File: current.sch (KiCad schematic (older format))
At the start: 35 parts

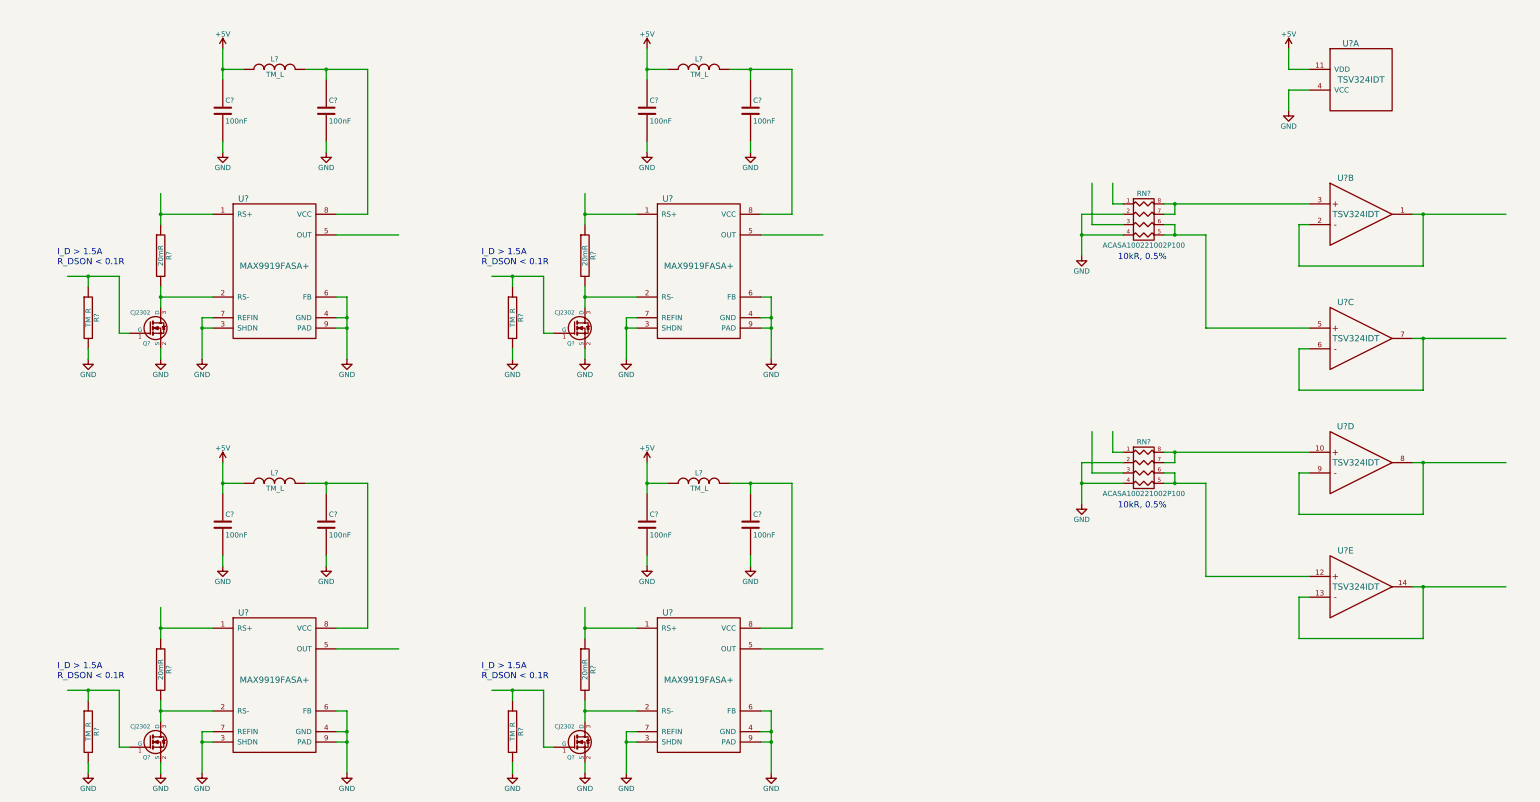
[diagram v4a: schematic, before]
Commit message: connected analog things, lots of testpoints
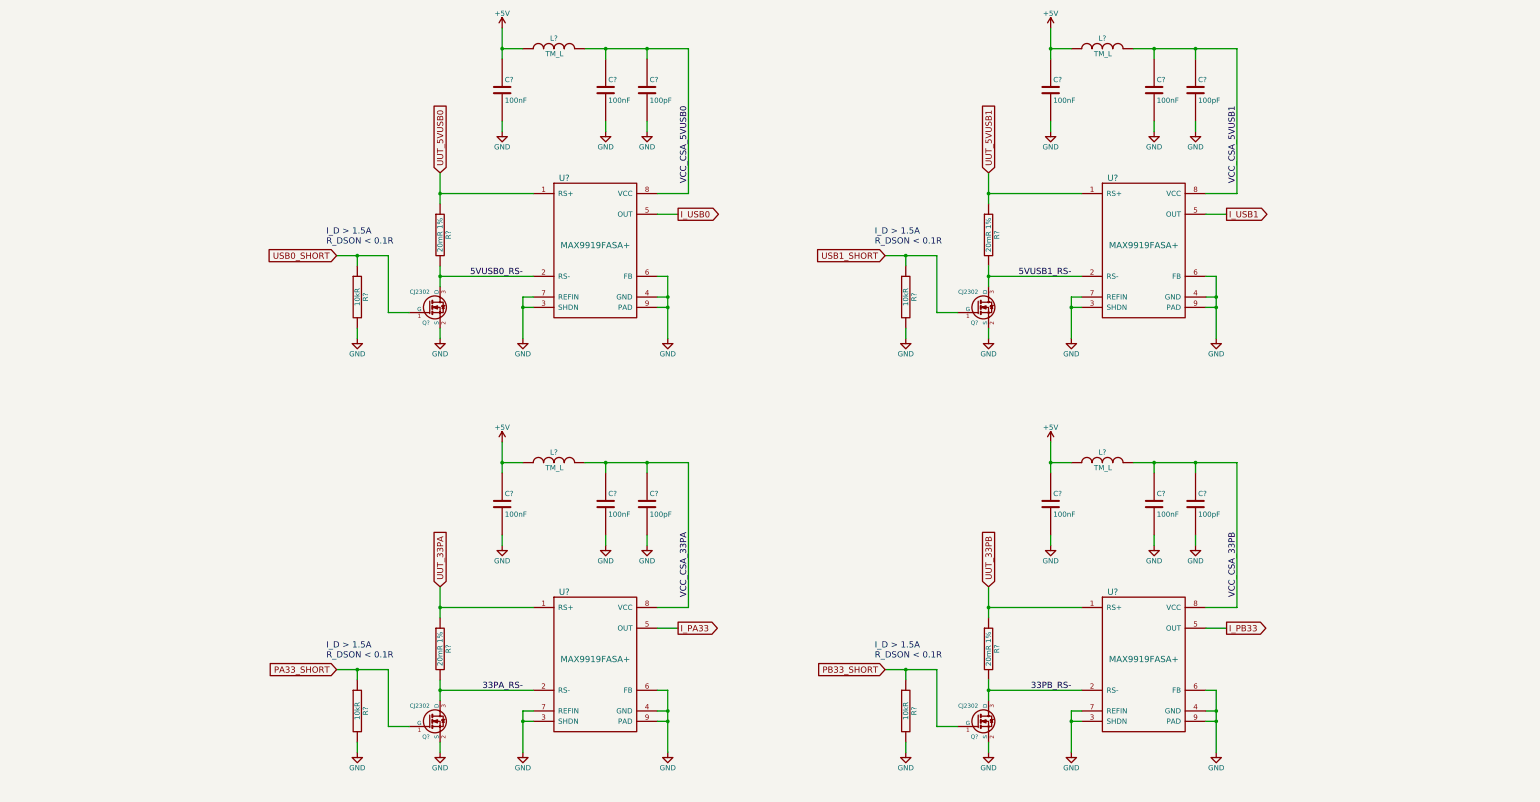
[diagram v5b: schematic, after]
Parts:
- removed C? (x6): 100nF, symbol TM_C
- removed L? (x3): TM_L, symbol TM_L
- removed RN? (x2): ACASA100221002P100, symbol R_PACK4
- removed U? (x5): TSV324IDT, symbol TSV324IDT
- added C? (x4): 100pF, symbol TM_C
- added C? (x6): 100nF, symbol TM_C
- added L? (x3): TM_L, symbol TM_L
- R? (x4): value 20mR -> 20mR 1%
- R? (x4): value TM_R -> 10kR
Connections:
- net labels added: 33PA_RS-, 33PB_RS-, 5VUSB0_RS-, 5VUSB1_RS-, I_PA33, I_PB33, I_USB0, I_USB1, PA33_SHORT, PB33_SHORT, USB0_SHORT, USB1_SHORT, UUT_33PA, UUT_33PB, UUT_5VUSB0, UUT_5VUSB1, VCC_CSA_33PA, VCC_CSA_33PB, VCC_CSA_5VUSB0, VCC_CSA_5VUSB1
- wire segments 158 -> 144
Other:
- note removed: "10kR, 0.5%"
- moved on the sheet: C?, L?, Q?, R?, U?

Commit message: schematic check with kevin. misc fixes, mostly on usb
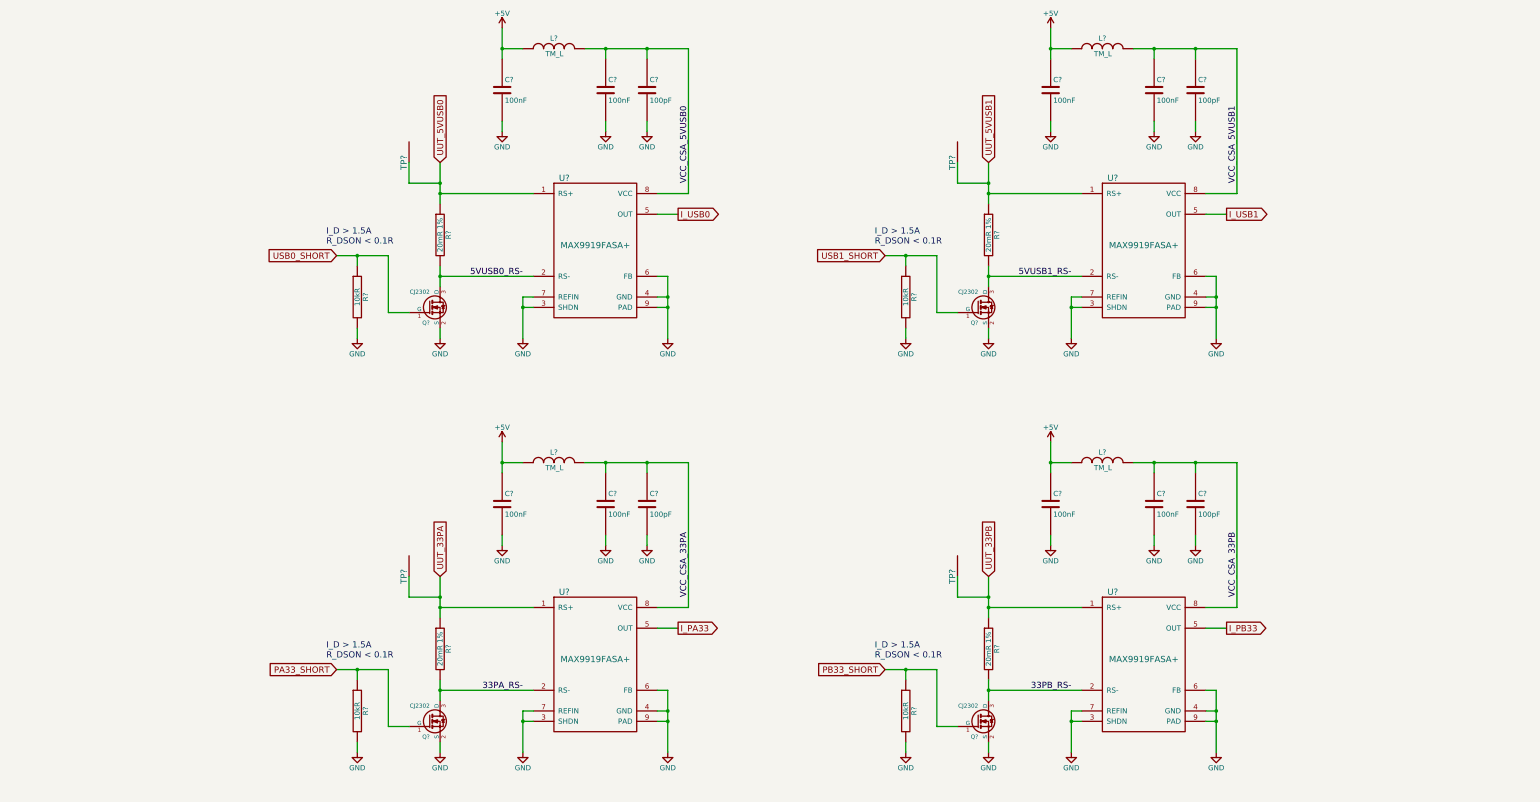
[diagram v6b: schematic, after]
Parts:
- added TP? (x4): TP, symbol TP
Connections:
- net UUT_33PA: now also TP?.~
- net UUT_33PB: now also TP?.~
- net UUT_5VUSB0: now also TP?.~
- net UUT_5VUSB1: now also TP?.~
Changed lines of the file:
@@
 	10600 3000 11500 3000
 Wire Wire Line
-	10600 2800 10600 3000
+	10600 2700 10600 2900
+Wire Wire Line
+	10600 2900 10600 3000
 Wire Wire Line
 	10600 3000 10600 3100
@@
 	5300 3000 6200 3000
 Wire Wire Line
-	5300 2800 5300 3000
+	5300 2700 5300 2900
+Wire Wire Line
+	5300 2900 5300 3000
 Wire Wire Line
 	5300 3000 5300 3100
@@
 	6700 1600 6900 1600
 Wire Wire Line
-	6900 1600 7700 1600
+	6900 1600 7300 1600
+Wire Wire Line
+	7300 1600 7700 1600
 Connection ~ 6900 1600
 Connection ~ 5300 3800
@@
 	5300 7000 6200 7000
 Wire Wire Line
-	5300 6800 5300 7000
+	5300 6700 5300 6900
+Wire Wire Line
+	5300 6900 5300 7000
 Wire Wire Line
 	5300 7000 5300 7100
@@
 	10600 7000 11500 7000
 Wire Wire Line
-	10600 6800 10600 7000
+	10600 6700 10600 6900
+Wire Wire Line
+	10600 6900 10600 7000
 Wire Wire Line
 	10600 7000 10600 7100
@@
 Text GLabel 9600 7600 0    60   Input ~ 0
 PB33_SHORT
-Text GLabel 5300 2800 1    60   Input ~ 0
+Text GLabel 5300 2700 1    60   Input ~ 0
 UUT_5VUSB0
-Text GLabel 10600 2800 1    60   Input ~ 0
+Text GLabel 10600 2700 1    60   Input ~ 0
 UUT_5VUSB1
-Text GLabel 5300 6800 1    60   Input ~ 0
+Text GLabel 5300 6700 1    60   Input ~ 0
 UUT_33PA
-Text GLabel 10600 6800 1    60   Input ~ 0
+Text GLabel 10600 6700 1    60   Input ~ 0
 UUT_33PB
 Text Label 6100 3800 2    60   ~ 0
@@
 	12000 1600 12200 1600
 Wire Wire Line
-	12200 1600 13000 1600
+	12200 1600 12600 1600
+Wire Wire Line
+	12600 1600 13000 1600
 Connection ~ 12200 1600
 Wire Wire Line
@@
 	12000 5600 12200 5600
 Wire Wire Line
-	12200 5600 13000 5600
+	12200 5600 12600 5600
+Wire Wire Line
+	12600 5600 13000 5600
 Connection ~ 12200 5600
 Wire Wire Line
@@
 	6700 5600 6900 5600
 Wire Wire Line
-	6900 5600 7700 5600
+	6900 5600 7300 5600
+Wire Wire Line
+	7300 5600 7700 5600
 Connection ~ 6900 5600
 Wire Wire Line
@@
 	7300 6400 7300 6300
 Connection ~ 7300 5600
+$Comp
+L TP TP?
+U 1 1 5541BEB7
+P 5000 2700
+F 0 "TP?" H 5000 2750 60  0000 C CNN
+F 1 "TP" H 5000 2650 60  0001 C CNN
+F 2 "" H 5000 2700 60  0000 C CNN
+F 3 "" H 5000 2700 60  0000 C CNN
+	1    5000 2700
+	0    -1   -1   0
+$EndComp
+Wire Wire Line
+	5000 2700 5000 2900
+Wire Wire Line
+	5000 2900 5300 2900
+Connection ~ 5300 2900
+$Comp
+L TP TP?
+U 1 1 5541C9E9
+P 10300 2700
+F 0 "TP?" H 10300 2750 60  0000 C CNN
+F 1 "TP" H 10300 2650 60  0001 C CNN
+F 2 "" H 10300 2700 60  0000 C CNN
+F 3 "" H 10300 2700 60  0000 C CNN
+	1    10300 2700
+	0    -1   -1   0
+$EndComp
+Wire Wire Line
+	10300 2700 10300 2900
+Wire Wire Line
+	10300 2900 10600 2900
+Connection ~ 10600 2900
+$Comp
+L TP TP?
+U 1 1 5541D870
+P 10300 6700
+F 0 "TP?" H 10300 6750 60  0000 C CNN
+F 1 "TP" H 10300 6650 60  0001 C CNN
+F 2 "" H 10300 6700 60  0000 C CNN
+F 3 "" H 10300 6700 60  0000 C CNN
+	1    10300 6700
+	0    -1   -1   0
+$EndComp
+Wire Wire Line
+	10300 6700 10300 6900
+Wire Wire Line
+	10300 6900 10600 6900
+Connection ~ 10600 6900
+$Comp
+L TP TP?
+U 1 1 5541E302
+P 5000 6700
+F 0 "TP?" H 5000 6750 60  0000 C CNN
+F 1 "TP" H 5000 6650 60  0001 C CNN
+F 2 "" H 5000 6700 60  0000 C CNN
+F 3 "" H 5000 6700 60  0000 C CNN
+	1    5000 6700
+	0    -1   -1   0
+$EndComp
+Wire Wire Line
+	5000 6700 5000 6900
+Wire Wire Line
+	5000 6900 5300 6900
+Connection ~ 5300 6900
 $EndSCHEMATC

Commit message: passed schematic review
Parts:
- removed L? (x3): TM_L, symbol TM_L
- added C? (x2): 100nF, symbol TM_C
- added C?: 100pF, symbol TM_C
- added L? (x4): 10uH, symbol TM_L
- added R?: 20mR 1%, symbol TM_R
- added U?: MAX9919FASA+, symbol MAX9919
- L?: value TM_L -> 10uH
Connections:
- net +5V: now also C?.1, L?.2, L?.2, L?.2, L?.2, R?.1, U?.1 (RS+)
- net GND: now also C?.2, C?.2, C?.2, U?.3 (SHDN), U?.4 (GND), U?.6 (FB), U?.7 (REFIN), U?.9 (PAD)
- net VCC_CSA_33PA: now also L?.1
- net VCC_CSA_33PB: now also L?.1
- net VCC_CSA_5VUSB1: now also L?.1
- net 5VUSB1_RS- renamed UUT_5V_UPSTREAM
- net UUT_5V_UPSTREAM: now also R?.2, U?.2 (RS-)
- new net I_UUT: U?.5 (OUT)
- new net VCC_CSA_UUT: C?.1, C?.1, L?.1, U?.8 (VCC)
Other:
- moved on the sheet: C?, L?, Q?, R?, TP?, U?
